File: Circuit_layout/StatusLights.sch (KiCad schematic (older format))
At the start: 12 parts

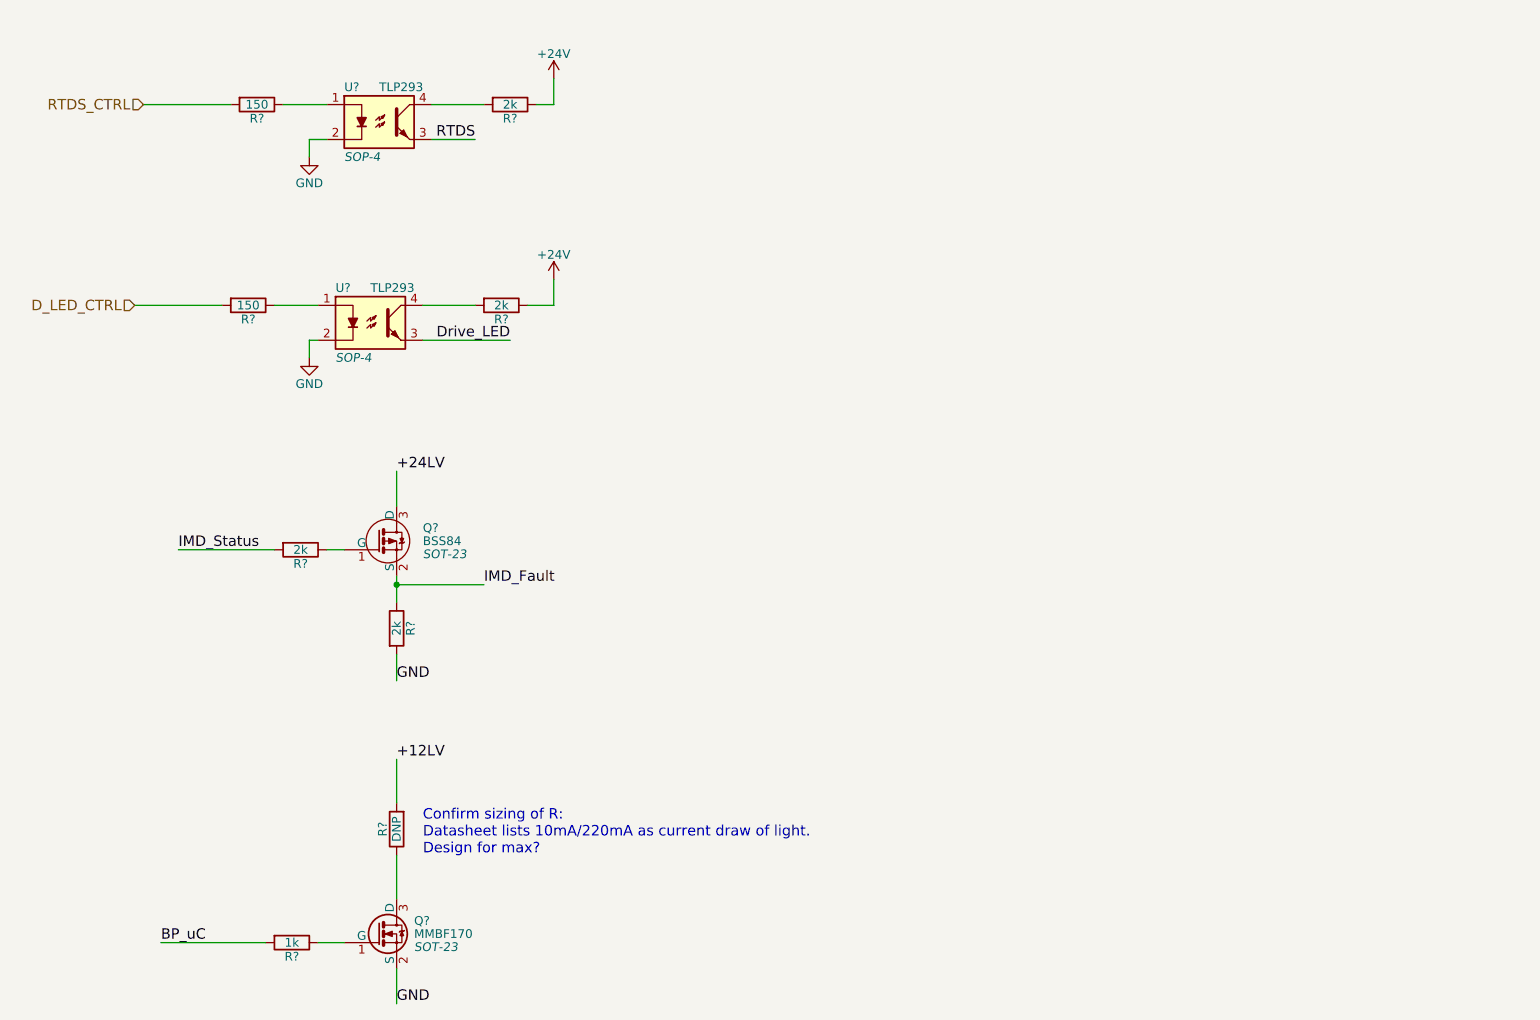
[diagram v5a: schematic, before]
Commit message: added debug LEDs and AIRs connections
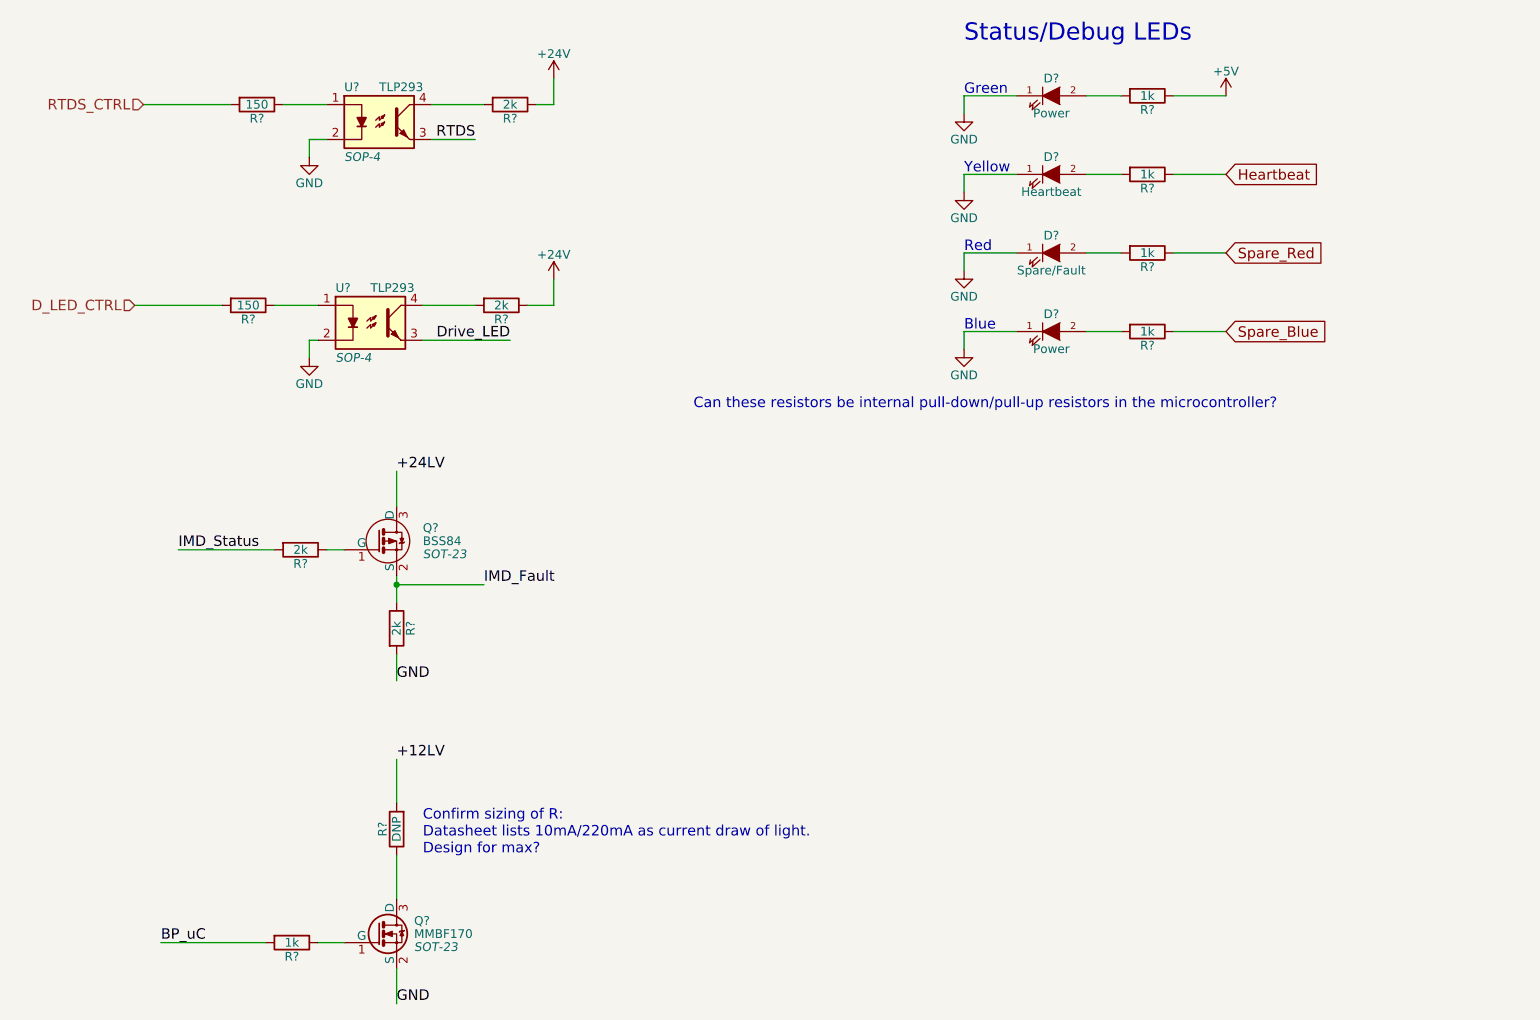
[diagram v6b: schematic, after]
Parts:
- added D? (x2): Power, LEDs:LED_0805, symbol LED
- added D?: Heartbeat, LEDs:LED_0805, symbol LED
- added D?: Spare/Fault, LEDs:LED_0805, symbol LED
- added R? (x4): 1k, Resistors_SMD:R_0805_HandSoldering, symbol R
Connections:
- net GND: now also D?.1 (K), D?.1 (K), D?.1 (K), D?.1 (K)
- new net: D?.2 (A), R?.2 (x4)
- new net +5V: R?.1
- new net Heartbeat: R?.1
- new net Spare_Blue: R?.1
- new net Spare_Red: R?.1
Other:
- note added: "Blue"
- note added: "Can these resistors be internal pull-down/pull-up resistors in the microcontroller?"
- note added: "Green"
- note added: "Red"
- note added: "Status/Debug LEDs"
- note added: "Yellow"
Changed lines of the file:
@@
 LIBS:xilinx
 LIBS:Zilog
-LIBS:pacman-main-cache
 LIBS:bss84
 LIBS:Circuit_layout-cache
@@
 	5150 4400 5250 4400
 Wire Wire Line
-	5550 4700 5550 4550
+	5550 4550 5550 4600
+Wire Wire Line
+	5550 4600 5550 4700
 Wire Wire Line
 	5550 4600 6050 4600
@@
 	1    0    0    -1
 $EndComp
+$Comp
+L R R?
+U 1 1 58B266DE
+P 9850 1800
+F 0 "R?" V 9930 1800 50  0000 C CNN
+F 1 "1k" V 9850 1800 50  0000 C CNN
+F 2 "Resistors_SMD:R_0805_HandSoldering" V 9780 1800 50  0001 C CNN
+F 3 "" H 9850 1800 50  0000 C CNN
+F 4 "P1.00KCCT-ND" V 9850 1800 60  0001 C CNN "DigiKey P/N"
+F 5 "http://www.digikey.com/product-detail/en/panasonic-electronic-components/ERJ-6ENF1001V/P1.00KCCT-ND/118957" V 9850 1800 60  0001 C CNN "URL"
+F 6 "ERJ-6ENF1001V" V 9850 1800 60  0001 C CNN "Man P/N"
+	1    9850 1800
+	0    1    1    0
+$EndComp
+$Comp
+L LED D?
+U 1 1 58B26743
+P 9300 1800
+F 0 "D?" H 9300 1900 50  0000 C CNN
+F 1 "Power" H 9300 1700 50  0000 C CNN
+F 2 "LEDs:LED_0805" H 9300 1800 50  0001 C CNN
+F 3 "" H 9300 1800 50  0000 C CNN
+F 4 "475-1410-1-ND" H 9300 1800 60  0001 C CNN "DigiKey P/N"
+F 5 "http://www.digikey.com/product-detail/en/osram-opto-semiconductors-inc/LG-R971-KN-1/475-1410-1-ND/1802598" H 9300 1800 60  0001 C CNN "URL"
+F 6 "LG R971-KN-1" H 9300 1800 60  0001 C CNN "Man P/N"
+	1    9300 1800
+	1    0    0    -1
+$EndComp
+Wire Wire Line
+	9500 1800 9700 1800
+Wire Wire Line
+	10000 1800 10300 1800
+Wire Wire Line
+	9100 1800 8800 1800
+Wire Wire Line
+	8800 1800 8800 1900
+$Comp
+L GND #PWR?
+U 1 1 58B26825
+P 8800 1900
+F 0 "#PWR?" H 8800 1650 50  0001 C CNN
+F 1 "GND" H 8800 1750 50  0000 C CNN
+F 2 "" H 8800 1900 50  0000 C CNN
+F 3 "" H 8800 1900 50  0000 C CNN
+	1    8800 1900
+	1    0    0    -1
+$EndComp
+Text Notes 8800 1800 0    60   ~ 0
+Green
+$Comp
+L LED D?
+U 1 1 58B26F44
+P 9300 2250
+F 0 "D?" H 9300 2350 50  0000 C CNN
+F 1 "Heartbeat" H 9300 2150 50  0000 C CNN
+F 2 "LEDs:LED_0805" H 9300 2250 50  0001 C CNN
+F 3 "" H 9300 2250 50  0000 C CNN
+F 4 "475-2560-1-ND" H 9300 2250 60  0001 C CNN "DigiKey P/N"
+F 5 "http://www.digikey.com/product-detail/en/osram-opto-semiconductors-inc/LY-R976-PS-36/475-2560-1-ND/1802687" H 9300 2250 60  0001 C CNN "URL"
+F 6 "LY R976-PS-36" H 9300 2250 60  0001 C CNN "Man P/N"
+	1    9300 2250
+	1    0    0    -1
+$EndComp
+Wire Wire Line
+	9500 2250 9700 2250
+Wire Wire Line
+	10000 2250 10300 2250
+Wire Wire Line
+	9100 2250 8800 2250
+Wire Wire Line
+	8800 2250 8800 2350
+$Comp
+L GND #PWR?
+U 1 1 58B26F4E
+P 8800 2350
+F 0 "#PWR?" H 8800 2100 50  0001 C CNN
+F 1 "GND" H 8800 2200 50  0000 C CNN
+F 2 "" H 8800 2350 50  0000 C CNN
+F 3 "" H 8800 2350 50  0000 C CNN
+	1    8800 2350
+	1    0    0    -1
+$EndComp
+Text Notes 8800 2250 0    60   ~ 0
+Yellow
+$Comp
+L LED D?
+U 1 1 58B272A0
+P 9300 2700
+F 0 "D?" H 9300 2800 50  0000 C CNN
+F 1 "Spare/Fault" H 9300 2600 50  0000 C CNN
+F 2 "LEDs:LED_0805" H 9300 2700 50  0001 C CNN
+F 3 "" H 9300 2700 50  0000 C CNN
+F 4 "475-1278-1-ND" H 9300 2700 60  0001 C CNN "DigiKey P/N"
+F 5 "http://www.digikey.com/product-detail/en/osram-opto-semiconductors-inc/LS-R976-NR-1/475-1278-1-ND/1642798" H 9300 2700 60  0001 C CNN "URL"
+F 6 "LS R976-NR-1" H 9300 2700 60  0001 C CNN "Man P/N"
+	1    9300 2700
+	1    0    0    -1
+$EndComp
+Wire Wire Line
+	9500 2700 9700 2700
+Wire Wire Line
+	10000 2700 10300 2700
+Wire Wire Line
+	9100 2700 8800 2700
+Wire Wire Line
+	8800 2700 8800 2800
+$Comp
+L GND #PWR?
+U 1 1 58B272AA
+P 8800 2800
+F 0 "#PWR?" H 8800 2550 50  0001 C CNN
+F 1 "GND" H 8800 2650 50  0000 C CNN
+F 2 "" H 8800 2800 50  0000 C CNN
+F 3 "" H 8800 2800 50  0000 C CNN
+	1    8800 2800
+	1    0    0    -1
+$EndComp
+Text Notes 8800 2700 0    60   ~ 0
+Red
+$Comp
+L LED D?
+U 1 1 58B27326
+P 9300 3150
+F 0 "D?" H 9300 3250 50  0000 C CNN
+F 1 "Power" H 9300 3050 50  0000 C CNN
+F 2 "LEDs:LED_0805" H 9300 3150 50  0001 C CNN
+F 3 "" H 9300 3150 50  0000 C CNN
+F 4 "516-1445-1-ND" H 9300 3150 60  0001 C CNN "DigiKey P/N"
+F 5 "http://www.digikey.com/product-detail/en/broadcom-limited/HSMR-C170/516-1445-1-ND/637769" H 9300 3150 60  0001 C CNN "URL"
+F 6 "HSMR-C170" H 9300 3150 60  0001 C CNN "Man P/N"
+	1    9300 3150
+	1    0    0    -1
+$EndComp
+Wire Wire Line
+	9500 3150 9700 3150
+Wire Wire Line
+	10000 3150 10300 3150
+Wire Wire Line
+	9100 3150 8800 3150
+Wire Wire Line
+	8800 3150 8800 3250
+$Comp
+L GND #PWR?
+U 1 1 58B27330
+P 8800 3250
+F 0 "#PWR?" H 8800 3000 50  0001 C CNN
+F 1 "GND" H 8800 3100 50  0000 C CNN
+F 2 "" H 8800 3250 50  0000 C CNN
+F 3 "" H 8800 3250 50  0000 C CNN
+	1    8800 3250
+	1    0    0    -1
+$EndComp
+Text Notes 8800 3150 0    60   ~ 0
+Blue
+$Comp
+L R R?
+U 1 1 58B27F91
+P 9850 2250
+F 0 "R?" V 9930 2250 50  0000 C CNN
+F 1 "1k" V 9850 2250 50  0000 C CNN
+F 2 "Resistors_SMD:R_0805_HandSoldering" V 9780 2250 50  0001 C CNN
+F 3 "" H 9850 2250 50  0000 C CNN
+F 4 "P1.00KCCT-ND" V 9850 2250 60  0001 C CNN "DigiKey P/N"
+F 5 "http://www.digikey.com/product-detail/en/panasonic-electronic-components/ERJ-6ENF1001V/P1.00KCCT-ND/118957" V 9850 2250 60  0001 C CNN "URL"
+F 6 "ERJ-6ENF1001V" V 9850 2250 60  0001 C CNN "Man P/N"
+	1    9850 2250
+	0    1    1    0
+$EndComp
+$Comp
+L R R?
+U 1 1 58B27FEF
+P 9850 2700
+F 0 "R?" V 9930 2700 50  0000 C CNN
+F 1 "1k" V 9850 2700 50  0000 C CNN
+F 2 "Resistors_SMD:R_0805_HandSoldering" V 9780 2700 50  0001 C CNN
+F 3 "" H 9850 2700 50  0000 C CNN
+F 4 "P1.00KCCT-ND" V 9850 2700 60  0001 C CNN "DigiKey P/N"
+F 5 "http://www.digikey.com/product-detail/en/panasonic-electronic-components/ERJ-6ENF1001V/P1.00KCCT-ND/118957" V 9850 2700 60  0001 C CNN "URL"
+F 6 "ERJ-6ENF1001V" V 9850 2700 60  0001 C CNN "Man P/N"
+	1    9850 2700
+	0    1    1    0
+$EndComp
+$Comp
+L R R?
+U 1 1 58B28050
+P 9850 3150
+F 0 "R?" V 9930 3150 50  0000 C CNN
+F 1 "1k" V 9850 3150 50  0000 C CNN
+F 2 "Resistors_SMD:R_0805_HandSoldering" V 9780 3150 50  0001 C CNN
+F 3 "" H 9850 3150 50  0000 C CNN
+F 4 "P1.00KCCT-ND" V 9850 3150 60  0001 C CNN "DigiKey P/N"
+F 5 "http://www.digikey.com/product-detail/en/panasonic-electronic-components/ERJ-6ENF1001V/P1.00KCCT-ND/118957" V 9850 3150 60  0001 C CNN "URL"
+F 6 "ERJ-6ENF1001V" V 9850 3150 60  0001 C CNN "Man P/N"
+	1    9850 3150
+	0    1    1    0
+$EndComp
+$Comp
+L +5V #PWR?
+U 1 1 58B2809B
+P 10300 1800
+F 0 "#PWR?" H 10300 1650 50  0001 C CNN
+F 1 "+5V" H 10300 1940 50  0000 C CNN
+F 2 "" H 10300 1800 50  0000 C CNN
+F 3 "" H 10300 1800 50  0000 C CNN
+	1    10300 1800
+	1    0    0    -1
+$EndComp
+Text GLabel 10300 2250 2    60   Input ~ 0
+Heartbeat
+Text GLabel 10300 2700 2    60   Input ~ 0
+Spare_Red
+Text GLabel 10300 3150 2    60   Input ~ 0
+Spare_Blue
+Text Notes 8800 1500 0    99   ~ 0
+Status/Debug LEDs
+Text Notes 7250 3600 0    60   ~ 0
+Can these resistors be internal pull-down/pull-up resistors in the microcontroller?
 $EndSCHEMATC

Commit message: filling out field info. for all added devices. think im done w/ resistors.
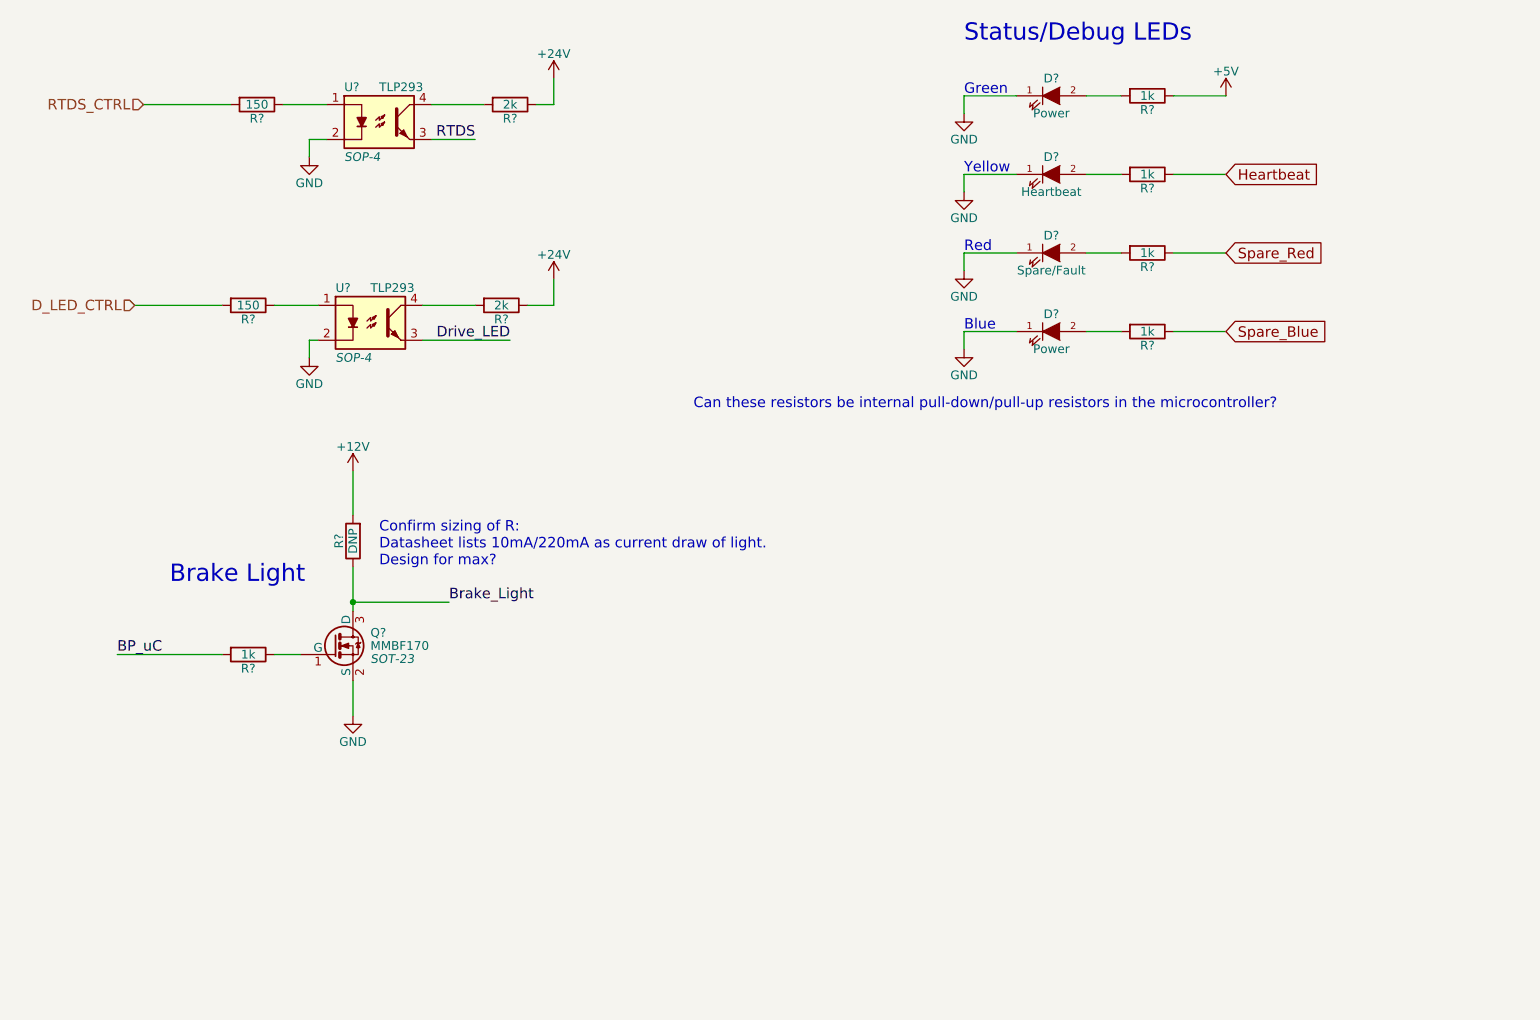
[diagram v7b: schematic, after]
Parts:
- removed Q?: BSS84, SOT-23, symbol BSS84
- removed R? (x2): 2k, symbol R
- removed R?: 1k, symbol R
- added R?: 1k, Resistors_SMD:R_0805_HandSoldering, symbol R
- R?: footprint (none) -> Resistors_SMD:R_0805_HandSoldering
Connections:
- net BP_uC: now also R?.2
- net at Q?.1 (G): now also R?.1
- net Brake_Light: now reaches Q?.3 (D), R?.1
- net +12LV renamed +12V
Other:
- note added: "Brake Light"
- moved on the sheet: Q?, R?
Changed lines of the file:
@@
 LIBS:xilinx
 LIBS:Zilog
+LIBS:pacman-main-cache
 LIBS:bss84
+LIBS:+10v
 LIBS:Circuit_layout-cache
 EELAYER 25 0
@@
 Text HLabel 4100 1850 0    60   Input ~ 0
 RTDS_CTRL
-Wire Wire Line
-	5550 4150 5550 3950
-$Comp
-L R R?
-U 1 1 58B1C4A9
-P 5550 4850
-F 0 "R?" V 5630 4850 50  0000 C CNN
-F 1 "2k" V 5550 4850 50  0000 C CNN
-F 2 "" V 5480 4850 50  0000 C CNN
-F 3 "" H 5550 4850 50  0000 C CNN
-	1    5550 4850
-	1    0    0    -1
-$EndComp
-$Comp
-L R R?
-U 1 1 58B1C51E
-P 5000 4400
-F 0 "R?" V 5080 4400 50  0000 C CNN
-F 1 "2k" V 5000 4400 50  0000 C CNN
-F 2 "" V 4930 4400 50  0000 C CNN
-F 3 "" H 5000 4400 50  0000 C CNN
-	1    5000 4400
-	0    1    1    0
-$EndComp
-Wire Wire Line
-	5150 4400 5250 4400
-Wire Wire Line
-	5550 4550 5550 4600
-Wire Wire Line
-	5550 4600 5550 4700
-Wire Wire Line
-	5550 4600 6050 4600
-Connection ~ 5550 4600
-Text Label 6050 4600 0    60   ~ 0
-IMD_Fault
-Text Label 4300 4400 0    60   ~ 0
-IMD_Status
-Wire Wire Line
-	4300 4400 4850 4400
-Text Label 5550 3950 0    60   ~ 0
-+24LV
-Wire Wire Line
-	5550 5000 5550 5150
-Text Label 5550 5150 0    60   ~ 0
-GND
-$Comp
-L R R?
-U 1 1 58B1EE45
-P 4950 6650
-F 0 "R?" V 5030 6650 50  0000 C CNN
-F 1 "1k" V 4950 6650 50  0000 C CNN
-F 2 "" V 4880 6650 50  0000 C CNN
-F 3 "" H 4950 6650 50  0000 C CNN
-	1    4950 6650
-	0    1    1    0
-$EndComp
 $Comp
 L R R?
 U 1 1 58B1EEB2
-P 5550 6000
-F 0 "R?" V 5630 6000 50  0000 C CNN
-F 1 "DNP" V 5550 6000 50  0000 C CNN
-F 2 "" V 5480 6000 50  0000 C CNN
-F 3 "" H 5550 6000 50  0000 C CNN
-	1    5550 6000
+P 5300 4350
+F 0 "R?" V 5380 4350 50  0000 C CNN
+F 1 "DNP" V 5300 4350 50  0000 C CNN
+F 2 "Resistors_SMD:R_0805_HandSoldering" V 5230 4350 50  0001 C CNN
+F 3 "" H 5300 4350 50  0000 C CNN
+	1    5300 4350
 	-1   0    0    1
 $EndComp
 Wire Wire Line
-	5550 6400 5550 6150
-Wire Wire Line
-	5250 6650 5100 6650
-Wire Wire Line
-	4800 6650 4200 6650
-Wire Wire Line
-	5550 5850 5550 5600
-Wire Wire Line
-	5550 6800 5550 7000
-Text Label 5550 5600 0    60   ~ 0
-+12LV
-Text Label 5550 7000 0    60   ~ 0
-GND
-Text Label 4200 6650 0    60   ~ 0
+	5300 4750 5300 4500
+Wire Wire Line
+	5000 5000 4850 5000
+Wire Wire Line
+	4550 5000 3950 5000
+Wire Wire Line
+	5300 4200 5300 3950
+Wire Wire Line
+	5300 5150 5300 5350
+Text Label 3950 5000 0    60   ~ 0
 BP_uC
-Text Notes 5700 6150 0    60   ~ 0
+Text Notes 5450 4500 0    60   ~ 0
 Confirm sizing of R:\nDatasheet lists 10mA/220mA as current draw of light.\nDesign for max?
 $Comp
 L MMBF170 Q?
 U 1 1 58B25E37
-P 5450 6600
-F 0 "Q?" H 5650 6675 50  0000 L CNN
-F 1 "MMBF170" H 5650 6600 50  0000 L CNN
-F 2 "SOT-23" H 5650 6525 50  0000 L CIN
-F 3 "" H 5450 6600 50  0000 L CNN
-	1    5450 6600
-	1    0    0    -1
-$EndComp
-$Comp
-L BSS84 Q?
-U 1 1 58B20C85
-P 5450 4350
-F 0 "Q?" H 5700 4425 50  0000 L CNN
-F 1 "BSS84" H 5700 4350 50  0000 L CNN
-F 2 "SOT-23" H 5700 4275 50  0000 L CIN
-F 3 "" H 5450 4350 50  0000 L CNN
-	1    5450 4350
+P 5200 4950
+F 0 "Q?" H 5400 5025 50  0000 L CNN
+F 1 "MMBF170" H 5400 4950 50  0000 L CNN
+F 2 "SOT-23" H 5400 4875 50  0000 L CIN
+F 3 "" H 5200 4950 50  0000 L CNN
+	1    5200 4950
 	1    0    0    -1
 $EndComp
@@
 Text Notes 7250 3600 0    60   ~ 0
 Can these resistors be internal pull-down/pull-up resistors in the microcontroller?
+$Comp
+L GND #PWR?
+U 1 1 58B21DFD
+P 5300 5350
+F 0 "#PWR?" H 5300 5100 50  0001 C CNN
+F 1 "GND" H 5300 5200 50  0000 C CNN
+F 2 "" H 5300 5350 50  0000 C CNN
+F 3 "" H 5300 5350 50  0000 C CNN
+	1    5300 5350
+	1    0    0    -1
+$EndComp
+Text Notes 4250 4600 0    99   ~ 0
+Brake Light
+Wire Wire Line
+	5300 4700 5850 4700
+Connection ~ 5300 4700
+Text Label 5850 4700 0    60   ~ 0
+Brake_Light
+$Comp
+L +12V #PWR?
+U 1 1 58B22590
+P 5300 3950
+F 0 "#PWR?" H 5300 3800 50  0001 C CNN
+F 1 "+12V" H 5300 4090 50  0000 C CNN
+F 2 "" H 5300 3950 50  0000 C CNN
+F 3 "" H 5300 3950 50  0000 C CNN
+	1    5300 3950
+	1    0    0    -1
+$EndComp
+$Comp
+L R R?
+U 1 1 58B5DC19
+P 4700 5000
+F 0 "R?" V 4780 5000 50  0000 C CNN
+F 1 "1k" V 4700 5000 50  0000 C CNN
+F 2 "Resistors_SMD:R_0805_HandSoldering" V 4630 5000 50  0001 C CNN
+F 3 "" H 4700 5000 50  0000 C CNN
+F 4 "P1.00KCCT-ND" V 4700 5000 60  0001 C CNN "DigiKey P/N"
+F 5 "http://www.digikey.com/product-detail/en/panasonic-electronic-components/ERJ-6ENF1001V/P1.00KCCT-ND/118957" V 4700 5000 60  0001 C CNN "URL"
+F 6 "ERJ-6ENF1001V" V 4700 5000 60  0001 C CNN "Man P/N"
+	1    4700 5000
+	0    1    1    0
+$EndComp
 $EndSCHEMATC
